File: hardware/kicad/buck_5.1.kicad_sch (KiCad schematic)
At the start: 0 parts

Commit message: feat: added buck converter 12V to 5V
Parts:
- added C10, C11, C12: 10uF, symbol Device:C
- added C8, C9: 330uF, symbol Device:C
- added R10, R11: 100k, symbol Device:R
- added U2: LMZ23610TZ/NOPB, Buck-5V:NDY0011A_N, symbol Buck-5V:LMZ23610TZ_NOPB
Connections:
- new net: R10.2, R11.1, U2.7 (FB)
- new net GND_LOGIC: C10.2, C11.2, C12.2, C8.2, C9.2, R11.2, U2.5 (AGND), U2.6 (AGND)
- new net VIN: C10.1, C11.1, C12.1, U2.1 (VIN), U2.2 (VIN)
- new net VOUT: C8.1, C9.1, R10.1, U2.10 (VOUT), U2.11 (VOUT)

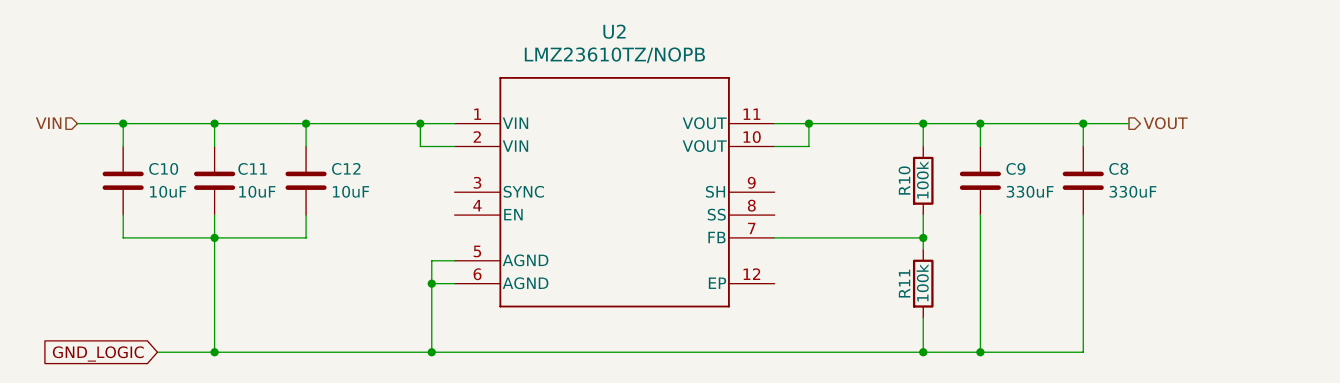
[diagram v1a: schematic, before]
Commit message: fix: footprint issues and library conflicts - KiCAD
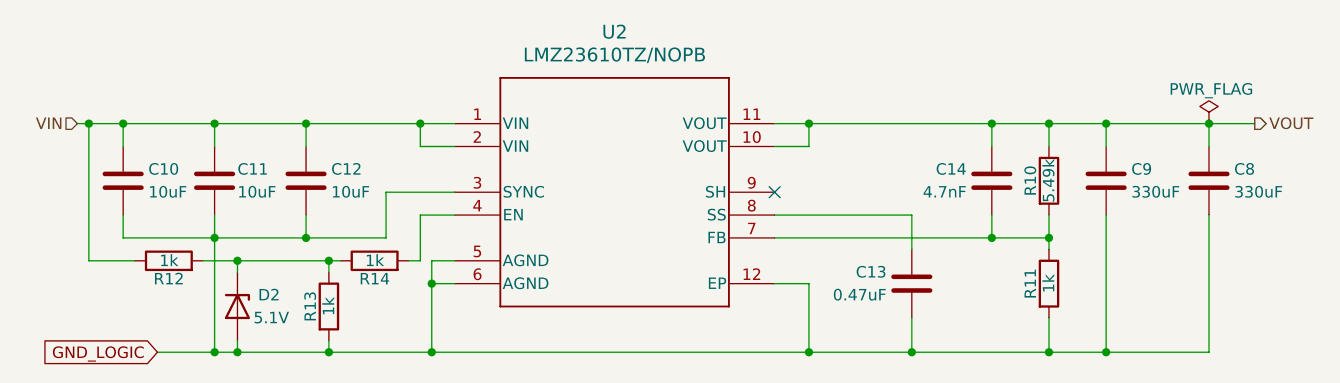
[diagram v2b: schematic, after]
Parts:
- added C13: 0.47uF, symbol Device:C
- added C14: 4.7nF, symbol Device:C
- added D2: 5.1V, symbol Device:D_Zener
- added R12, R13, R14: 1k, symbol Device:R
- R10: value 100k -> 5.49k
- R11: value 100k -> 1k
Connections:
- net GND_LOGIC: now also U2.12 (EP), U2.3 (SYNC), C13.2, D2.2 (A), R13.2
- net VIN: now also R12.1
- net VOUT: now also C14.1
- net at R10.2, R11.1, U2.7 (FB): now also C14.2
- net at U2.4 (EN): now also R14.2
- net at U2.8 (SS): now also C13.1
- new net: D2.1 (K), R12.2, R13.1, R14.1
- no-connect marks 0 -> 1
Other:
- moved on the sheet: C8, C9, R10, R11

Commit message: fix: protection circuit - MOSFET & enable config
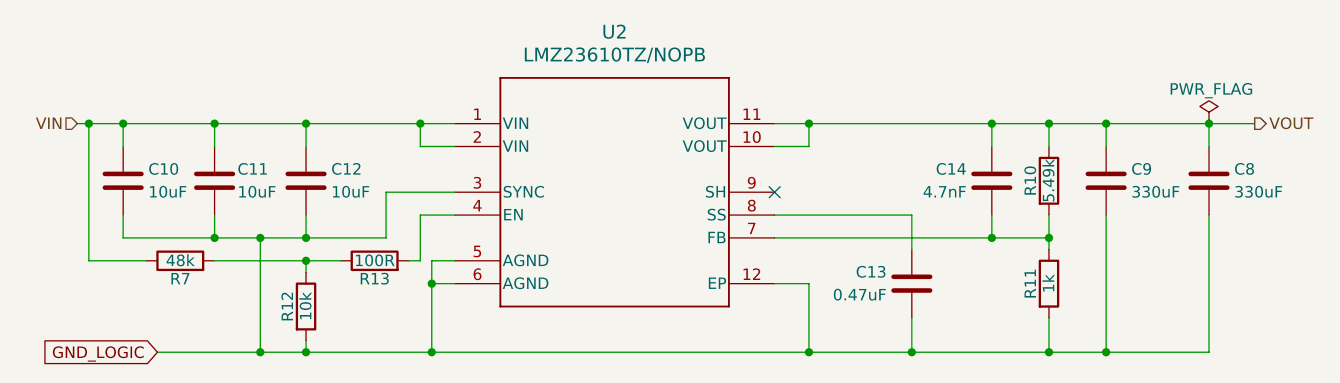
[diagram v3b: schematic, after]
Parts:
- removed D2: 5.1V, symbol Device:D_Zener
- removed R14: 1k, symbol Device:R
- added R7: 48k, symbol Device:R
- R12: value 1k -> 10k
- R13: value 1k -> 100R
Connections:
- net GND_LOGIC: now also R12.2; no longer R13.2
- net VIN: now also R7.1; no longer R12.1
- net at R13.1: now also R12.1, R7.2; no longer R12.2
- net at U2.4 (EN): now also R13.2

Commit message: feat: separated modules but added power module
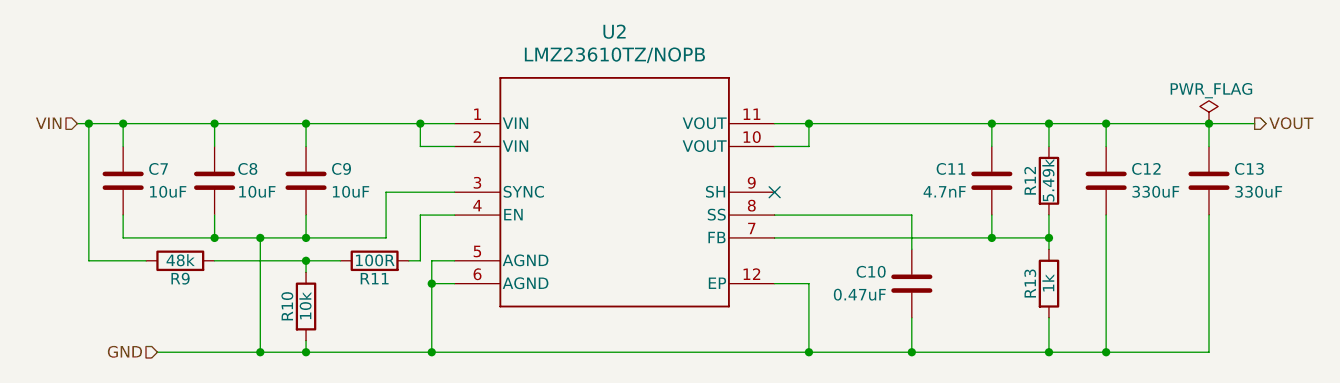
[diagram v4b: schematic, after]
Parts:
- C10: renamed from C13; footprint (none) -> Capacitor_THT:C_Rect_L4.6mm_W3.0mm_P2.50mm_MKS02_FKP02
- C11: renamed from C14; footprint (none) -> Capacitor_THT:C_Rect_L4.6mm_W3.0mm_P2.50mm_MKS02_FKP02
- C12: renamed from C9; footprint (none) -> Capacitor_THT:C_Rect_L28.0mm_W8.0mm_P22.50mm_MKS4
- C13: renamed from C8; footprint (none) -> Capacitor_THT:C_Rect_L28.0mm_W8.0mm_P22.50mm_MKS4
- C7: renamed from C10; footprint (none) -> Capacitor_THT:C_Rect_L4.0mm_W2.5mm_P2.50mm
- C8: renamed from C11; footprint (none) -> Capacitor_THT:C_Rect_L4.0mm_W2.5mm_P2.50mm
- C9: renamed from C12; footprint (none) -> Capacitor_THT:C_Rect_L4.0mm_W2.5mm_P2.50mm
- R10: renamed from R12; footprint (none) -> Resistor_THT:R_Axial_DIN0207_L6.3mm_D2.5mm_P2.54mm_Vertical
- R11: renamed from R13; footprint (none) -> Resistor_THT:R_Axial_DIN0207_L6.3mm_D2.5mm_P2.54mm_Vertical
- R12: renamed from R10; footprint (none) -> Resistor_THT:R_Axial_DIN0207_L6.3mm_D2.5mm_P2.54mm_Vertical
- R13: renamed from R11; footprint (none) -> Resistor_THT:R_Axial_DIN0207_L6.3mm_D2.5mm_P2.54mm_Vertical
- R9: renamed from R7; footprint (none) -> Resistor_THT:R_Axial_DIN0207_L6.3mm_D2.5mm_P2.54mm_Vertical
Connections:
- net GND_LOGIC renamed GND
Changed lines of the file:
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@@
-		)
-	)
-	(global_label "GND_LOGIC"
-		(shape input)
-		(at 66.04 92.71 180)
-		(fields_autoplaced yes)
-		(effects
-			(font
-				(size 1.27 1.27)
-			)
-			(justify right)
-		)
-		(property "Intersheetrefs" "${INTERSHEET_REFS}"
-			(at 52.7133 92.71 0)
-			(effects
-				(font
-					(size 1.27 1.27)
-				)
-				(justify right)
-				(hide yes)
-			)
 		)
 	)
@@
 		)
 	)
+	(hierarchical_label "GND"
+		(shape input)
+		(at 66.04 92.71 180)
+		(effects
+			(font
+				(size 1.27 1.27)
+			)
+			(justify right)
+		)
+	)
 	(symbol
 		(lib_id "Device:R")
@@
 		(on_board yes)
 		(dnp no)
-		(property "Reference" "R12"
+		(property "Reference" "R10"
 			(at 80.518 87.63 90)
 			(effects
@@
 			)
 		)
-		(property "Footprint" ""
+		(property "Footprint" "Resistor_THT:R_Axial_DIN0207_L6.3mm_D2.5mm_P2.54mm_Vertical"
 			(at 80.772 87.63 90)
 			(effects
@@
 		)
 		(instances
-			(project "card_issuance"
-				(path "/efd10ce8-d30e-4563-b475-2afafc95cd2b/d6ed446d-e13a-4330-af37-f0669133989b/5501bdb0-d5d4-479d-8ea5-83139bf20e95"
-					(reference "R12")
+			(project "card_issuance_power"
+				(path "/eccaacbb-6cc6-4795-9ce3-6b61aaecb3e3/8cc712a2-9e33-4f10-9d4a-c0c2a2a628a9"
+					(reference "R10")
 					(unit 1)
 				)
@@
 		(on_board yes)
 		(dnp no)
-		(property "Reference" "C8"
+		(property "Reference" "C13"
 			(at 185.674 72.39 0)
 			(effects
@@
 			)
 		)
-		(property "Footprint" ""
+		(property "Footprint" "Capacitor_THT:C_Rect_L28.0mm_W8.0mm_P22.50mm_MKS4"
 			(at 183.8452 77.47 0)
 			(effects
@@
 		)
 		(instances
-			(project ""
-				(path "/efd10ce8-d30e-4563-b475-2afafc95cd2b/d6ed446d-e13a-4330-af37-f0669133989b/5501bdb0-d5d4-479d-8ea5-83139bf20e95"
-					(reference "C8")
+			(project "card_issuance_power"
+				(path "/eccaacbb-6cc6-4795-9ce3-6b61aaecb3e3/8cc712a2-9e33-4f10-9d4a-c0c2a2a628a9"
+					(reference "C13")
 					(unit 1)
 				)
@@
 		(on_board yes)
 		(dnp no)
-		(property "Reference" "C9"
+		(property "Reference" "C12"
 			(at 174.244 72.39 0)
 			(effects
@@
 			)
 		)
-		(property "Footprint" ""
+		(property "Footprint" "Capacitor_THT:C_Rect_L28.0mm_W8.0mm_P22.50mm_MKS4"
 			(at 172.4152 77.47 0)
 			(effects
@@
 		)
 		(instances
-			(project ""
-				(path "/efd10ce8-d30e-4563-b475-2afafc95cd2b/d6ed446d-e13a-4330-af37-f0669133989b/5501bdb0-d5d4-479d-8ea5-83139bf20e95"
-					(reference "C9")
+			(project "card_issuance_power"
+				(path "/eccaacbb-6cc6-4795-9ce3-6b61aaecb3e3/8cc712a2-9e33-4f10-9d4a-c0c2a2a628a9"
+					(reference "C12")
 					(unit 1)
 				)
@@
 		(on_board yes)
 		(dnp no)
-		(property "Reference" "C12"
+		(property "Reference" "C9"
 			(at 85.344 72.39 0)
 			(effects
@@
 			)
 		)
-		(property "Footprint" ""
+		(property "Footprint" "Capacitor_THT:C_Rect_L4.0mm_W2.5mm_P2.50mm"
 			(at 83.5152 77.47 0)
 			(effects
@@
 		)
 		(instances
-			(project ""
-				(path "/efd10ce8-d30e-4563-b475-2afafc95cd2b/d6ed446d-e13a-4330-af37-f0669133989b/5501bdb0-d5d4-479d-8ea5-83139bf20e95"
-					(reference "C12")
+			(project "card_issuance_power"
+				(path "/eccaacbb-6cc6-4795-9ce3-6b61aaecb3e3/8cc712a2-9e33-4f10-9d4a-c0c2a2a628a9"
+					(reference "C9")
 					(unit 1)
 				)
@@
 		(on_board yes)
 		(dnp no)
-		(property "Reference" "C14"
+		(property "Reference" "C11"
 			(at 155.956 72.39 0)
 			(effects
@@
 			)
 		)
-		(property "Footprint" ""
+		(property "Footprint" "Capacitor_THT:C_Rect_L4.6mm_W3.0mm_P2.50mm_MKS02_FKP02"
 			(at 157.7848 77.47 0)
 			(effects
@@
 		)
 		(instances
-			(project "card_issuance"
-				(path "/efd10ce8-d30e-4563-b475-2afafc95cd2b/d6ed446d-e13a-4330-af37-f0669133989b/5501bdb0-d5d4-479d-8ea5-83139bf20e95"
-					(reference "C14")
+			(project "card_issuance_power"
+				(path "/eccaacbb-6cc6-4795-9ce3-6b61aaecb3e3/8cc712a2-9e33-4f10-9d4a-c0c2a2a628a9"
+					(reference "C11")
 					(unit 1)
 				)
@@
 		(on_board yes)
 		(dnp no)
-		(property "Reference" "R10"
+		(property "Reference" "R12"
 			(at 163.068 73.66 90)
 			(effects
@@
 			)
 		)
-		(property "Footprint" ""
+		(property "Footprint" "Resistor_THT:R_Axial_DIN0207_L6.3mm_D2.5mm_P2.54mm_Vertical"
 			(at 163.322 73.66 90)
 			(effects
@@
 		)
 		(instances
-			(project "card_issuance"
-				(path "/efd10ce8-d30e-4563-b475-2afafc95cd2b/d6ed446d-e13a-4330-af37-f0669133989b/5501bdb0-d5d4-479d-8ea5-83139bf20e95"
-					(reference "R10")
+			(project "card_issuance_power"
+				(path "/eccaacbb-6cc6-4795-9ce3-6b61aaecb3e3/8cc712a2-9e33-4f10-9d4a-c0c2a2a628a9"
+					(reference "R12")
 					(unit 1)
 				)
@@
 		(on_board yes)
 		(dnp no)
-		(property "Reference" "R11"
+		(property "Reference" "R13"
 			(at 163.068 85.09 90)
 			(effects
@@
 			)
 		)
-		(property "Footprint" ""
+		(property "Footprint" "Resistor_THT:R_Axial_DIN0207_L6.3mm_D2.5mm_P2.54mm_Vertical"
 			(at 163.322 85.09 90)
 			(effects
@@
 		)
 		(instances
-			(project "card_issuance"
-				(path "/efd10ce8-d30e-4563-b475-2afafc95cd2b/d6ed446d-e13a-4330-af37-f0669133989b/5501bdb0-d5d4-479d-8ea5-83139bf20e95"
-					(reference "R11")
+			(project "card_issuance_power"
+				(path "/eccaacbb-6cc6-4795-9ce3-6b61aaecb3e3/8cc712a2-9e33-4f10-9d4a-c0c2a2a628a9"
+					(reference "R13")
 					(unit 1)
 				)
@@
 		)
 		(instances
-			(project ""
-				(path "/efd10ce8-d30e-4563-b475-2afafc95cd2b/d6ed446d-e13a-4330-af37-f0669133989b/5501bdb0-d5d4-479d-8ea5-83139bf20e95"
+			(project "card_issuance_power"
+				(path "/eccaacbb-6cc6-4795-9ce3-6b61aaecb3e3/8cc712a2-9e33-4f10-9d4a-c0c2a2a628a9"
 					(reference "#FLG03")
 					(unit 1)
@@
 		(on_board yes)
 		(dnp no)
-		(property "Reference" "R7"
+		(property "Reference" "R9"
 			(at 68.58 84.582 90)
 			(effects
@@
 			)
 		)
-		(property "Footprint" ""
+		(property "Footprint" "Resistor_THT:R_Axial_DIN0207_L6.3mm_D2.5mm_P2.54mm_Vertical"
 			(at 68.58 84.328 90)
 			(effects
@@
 		)
 		(instances
-			(project "card_issuance"
-				(path "/efd10ce8-d30e-4563-b475-2afafc95cd2b/d6ed446d-e13a-4330-af37-f0669133989b/5501bdb0-d5d4-479d-8ea5-83139bf20e95"
-					(reference "R7")
+			(project "card_issuance_power"
+				(path "/eccaacbb-6cc6-4795-9ce3-6b61aaecb3e3/8cc712a2-9e33-4f10-9d4a-c0c2a2a628a9"
+					(reference "R9")
 					(unit 1)
 				)
@@
 		)
 		(instances
-			(project ""
-				(path "/efd10ce8-d30e-4563-b475-2afafc95cd2b/d6ed446d-e13a-4330-af37-f0669133989b/5501bdb0-d5d4-479d-8ea5-83139bf20e95"
+			(project "card_issuance_power"
+				(path "/eccaacbb-6cc6-4795-9ce3-6b61aaecb3e3/8cc712a2-9e33-4f10-9d4a-c0c2a2a628a9"
 					(reference "U2")
 					(unit 1)
@@
 		(on_board yes)
 		(dnp no)
-		(property "Reference" "C13"
+		(property "Reference" "C10"
 			(at 147.066 83.82 0)
 			(effects
@@
 			)
 		)
-		(property "Footprint" ""
+		(property "Footprint" "Capacitor_THT:C_Rect_L4.6mm_W3.0mm_P2.50mm_MKS02_FKP02"
 			(at 148.8948 88.9 0)
 			(effects
@@
 		)
 		(instances
-			(project "card_issuance"
-				(path "/efd10ce8-d30e-4563-b475-2afafc95cd2b/d6ed446d-e13a-4330-af37-f0669133989b/5501bdb0-d5d4-479d-8ea5-83139bf20e95"
-					(reference "C13")
+			(project "card_issuance_power"
+				(path "/eccaacbb-6cc6-4795-9ce3-6b61aaecb3e3/8cc712a2-9e33-4f10-9d4a-c0c2a2a628a9"
+					(reference "C10")
 					(unit 1)
 				)
@@
 		(on_board yes)
 		(dnp no)
-		(property "Reference" "R13"
+		(property "Reference" "R11"
 			(at 90.17 84.582 90)
 			(effects
@@
 			)
 		)
-		(property "Footprint" ""
+		(property "Footprint" "Resistor_THT:R_Axial_DIN0207_L6.3mm_D2.5mm_P2.54mm_Vertical"
 			(at 90.17 84.328 90)
 			(effects
@@
 		)
 		(instances
-			(project "card_issuance"
-				(path "/efd10ce8-d30e-4563-b475-2afafc95cd2b/d6ed446d-e13a-4330-af37-f0669133989b/5501bdb0-d5d4-479d-8ea5-83139bf20e95"
-					(reference "R13")
+			(project "card_issuance_power"
+				(path "/eccaacbb-6cc6-4795-9ce3-6b61aaecb3e3/8cc712a2-9e33-4f10-9d4a-c0c2a2a628a9"
+					(reference "R11")
 					(unit 1)
 				)
@@
 		(on_board yes)
 		(dnp no)
-		(property "Reference" "C11"
+		(property "Reference" "C8"
 			(at 74.93 72.39 0)
 			(effects
@@
 			)
 		)
-		(property "Footprint" ""
+		(property "Footprint" "Capacitor_THT:C_Rect_L4.0mm_W2.5mm_P2.50mm"
 			(at 73.3552 77.47 0)
 			(effects
@@
 		)
 		(instances
-			(project ""
-				(path "/efd10ce8-d30e-4563-b475-2afafc95cd2b/d6ed446d-e13a-4330-af37-f0669133989b/5501bdb0-d5d4-479d-8ea5-83139bf20e95"
-					(reference "C11")
+			(project "card_issuance_power"
+				(path "/eccaacbb-6cc6-4795-9ce3-6b61aaecb3e3/8cc712a2-9e33-4f10-9d4a-c0c2a2a628a9"
+					(reference "C8")
 					(unit 1)
 				)
@@
 		(on_board yes)
 		(dnp no)
-		(property "Reference" "C10"
+		(property "Reference" "C7"
 			(at 65.024 72.39 0)
 			(effects
@@
 			)
 		)
-		(property "Footprint" ""
+		(property "Footprint" "Capacitor_THT:C_Rect_L4.0mm_W2.5mm_P2.50mm"
 			(at 63.1952 77.47 0)
 			(effects
@@
 		)
 		(instances
-			(project ""
-				(path "/efd10ce8-d30e-4563-b475-2afafc95cd2b/d6ed446d-e13a-4330-af37-f0669133989b/5501bdb0-d5d4-479d-8ea5-83139bf20e95"
-					(reference "C10")
-					(unit 1)
-				)
+			(project "card_issuance_power"
+				(path "/eccaacbb-6cc6-4795-9ce3-6b61aaecb3e3/8cc712a2-9e33-4f10-9d4a-c0c2a2a628a9"
+					(reference "C7")
+					(unit 1)
+				)

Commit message: fix: buck connections
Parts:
- U2: footprint Buck-5V:NDY0011A_N -> Buck 5V:NDY0011A_N
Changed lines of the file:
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@@
 			)
 		)
-		(property "Footprint" "Buck-5V:NDY0011A_N"
+		(property "Footprint" "Buck 5V:NDY0011A_N"
 			(at 116.84 74.93 0)
 			(effects
